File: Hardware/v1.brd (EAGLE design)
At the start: 77.5 x 32.6 mm, 64 parts, among them CN1 629105150521, CN2 TSW-120-08-L-S-RA, CN3 1734354-1, CN4 1-1734530-1, IC1 ADUM3160BRWZ, IC2 TUSB2046BIRHBT, IC3 IC_MAX3313, IC4 FT2232D, IC6 PCM2903C

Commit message: fixed some silkscreen issues
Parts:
- moved IC6 58.6 mm to (7.30, 24.9)
- moved R7 57.1 mm to (13.8, 28.1), turned to 0 degrees
- moved R6 41.8 mm to (13.8, 29.4), turned to 0 degrees
- moved C11 0.20 mm to (60.8, 24.9)
- moved C25 0.20 mm to (30.6, 27.4)
- moved C27 0.20 mm to (47.1, 30.9)
- moved C28 0.20 mm to (30.6, 24.9)
- moved R11 0.20 mm to (47.1, 23.9)
- moved C10 0.20 mm to (53.6, 29.7)
- moved C26 0.20 mm to (47.1, 26.7)
- moved C8 0.20 mm to (58.2, 24.1)
- moved C9 0.20 mm to (51.0, 29.7)
- moved IC2 0.20 mm to (52.4, 25.5)
- moved IC4 0.20 mm to (37.2, 26.5)
- moved R10 0.20 mm to (47.1, 22.5)
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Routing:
- net USB4_N: track 0.00 -> 43.5 mm, vias 0 -> 2
- net USB4_P: track 0.00 -> 43.0 mm, vias 0 -> 2
- net GND: track 22.9 -> 31.2 mm, vias 24 -> 32
- net DM4: track 0.00 -> 2.35 mm
- net DP4: track 0.00 -> 2.31 mm
- net ACC_COMMON: track 34.9 -> 34.1 mm

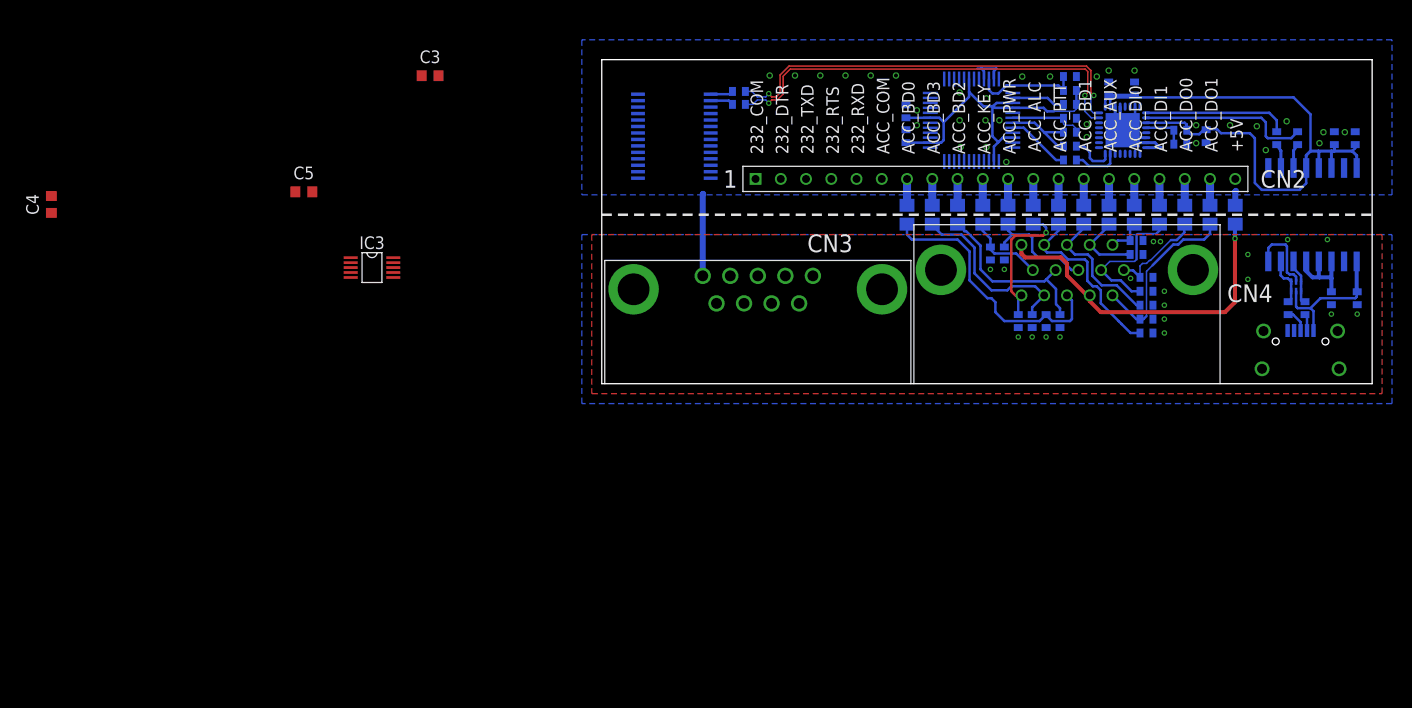
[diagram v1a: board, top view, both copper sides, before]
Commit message: added missing pullups to band lines
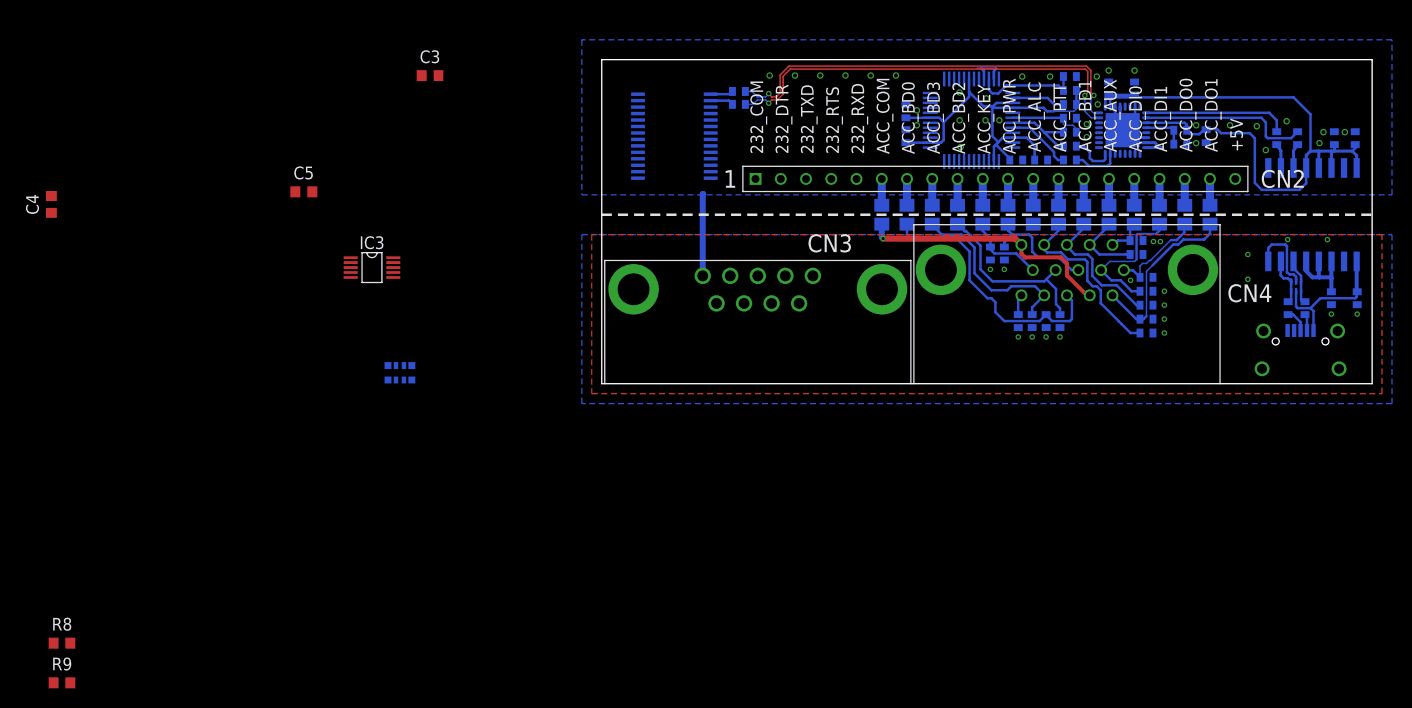
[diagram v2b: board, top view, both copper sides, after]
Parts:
- added C29: 100nF, rcl:C0402
- added C30: 1uF, rcl:C0402
- added R8: 69k8, rcl:R0603
- added R9: 100k, rcl:R0603
- added RN1: 2k2, m0wut:R_BOURNS_CAY16-J4
- C7: value 1uF -> 100nF
- moved L1 35.6 mm to (28.2, 17.0)
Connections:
- net +5V: now also C29.1, C30.1, R8.2, RN1.1, RN1.2, RN1.3, RN1.4
- net ACC_ALC: now also R9.2
- net ACC_BND0: now also RN1.3A
- net ACC_BND1: now also RN1.1A
- net ACC_BND2: now also RN1.2A
- net ACC_BND3: now also RN1.4A
- net ACC_COM: now also L1.1
- net GND: now also C29.2, C30.2, R9.1; no longer L1.1
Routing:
- net ALC_X: track 14.2 -> 2.07 mm, vias 1 -> 0
- net ACC_COMMON: track 34.1 -> 25.9 mm
- net +5V: track 38.4 -> 44.5 mm
- net ACC_COM: track 0.00 -> 2.65 mm
- net GND: track 31.2 -> 29.7 mm, vias 32 -> 31

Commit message: complete apart from sound card and PIC
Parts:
- added C31: 1uF, rcl:C0402
- added C32: 100nF, rcl:C0402
- C25: value 100nF -> 1uF
- C30: value 1uF -> 100nF
- R8, R9: device rcl:R0603 -> rcl:R0402
- moved R9 111.8 mm to (44.4, 22.5), flipped to the bottom
- moved R8 107.6 mm to (41.7, 22.5), flipped to the bottom
- moved RN1 53.0 mm to (27.5, 24.0), turned to 180 degrees
- moved C29 5.60 mm to (44.4, 28.1)
- moved C30 3.04 mm to (44.4, 23.9)
- moved R6 1.05 mm to (13.8, 30.4)
- moved R7 1.05 mm to (13.8, 29.1)
- moved IC6 1.00 mm to (7.30, 25.9)
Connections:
- net +5V: now also C31.1, C32.1
- net ACC_ALC: now also R8.1
- net ACC_BND0: now also RN1.1A; no longer RN1.3A
- net ACC_BND1: now also RN1.4A; no longer RN1.1A
- net ACC_BND2: now also RN1.3A; no longer RN1.2A
- net ACC_BND3: now also RN1.2A; no longer RN1.4A
- net GND: now also C31.2, C32.2
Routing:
- net ALC_X: track 2.07 -> 23.5 mm, vias 0 -> 1
- net ACC_BND1: track 2.65 -> 23.5 mm, vias 0 -> 1
- net +5V: track 44.5 -> 55.6 mm
- net ACC_BND2: track 2.65 -> 12.0 mm
- net ACC_BND3: track 2.65 -> 10.5 mm
- net ACC_BND0: track 2.65 -> 8.86 mm
- net ACC_ALC: track 2.65 -> 7.03 mm
- net DP2: track 8.02 -> 6.89 mm
- net USB4_P: track 43.0 -> 41.9 mm
- net USB4_N: track 43.5 -> 42.4 mm
- net N$37: track 5.37 -> 6.40 mm
- net DM2: track 6.68 -> 7.60 mm
- net GND: vias 31 -> 32
- added copper zone on layer 1, net GND

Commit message: destruction in the name of progress...
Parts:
- removed C3, C4, C5: 100nF, rcl:C0603
- removed IC6: PCM2903C, texas:SSOP28DB
- added C33, C34: 1nF, rcl:C0402
- added CAN1: SHIELDING_CAN, m0wut:CAN_LEADER_SMS462
- added D2: BZT52C3V0-7-F, adafruit:SOD-123
- added L2, L3, L4, L5, L6, L7: 100uH, m0wut:R0805
- added R12: 220, rcl:R0402
- CN1: value 629105150521 -> 54819-0519; device m0wut:USB_MICROB_WURTH -> m0wut:CONN_USB_MOLEX_MINI
- IC3: value IC_MAX3313 -> (none); device m0wut:IC_UMAX10 -> m0wut:SOT23-8L
- moved IC3 42.2 mm to (17.0, 24.9), flipped to the bottom, turned to 90 degrees
- moved R6 7.85 mm to (19.2, 36.1)
- moved R7 6.51 mm to (14.2, 35.6)
- moved C11 3.85 mm to (64.7, 24.9)
- moved C10 3.85 mm to (57.5, 29.7)
- moved C25 3.85 mm to (34.5, 27.4)
- moved C26 3.85 mm to (51.0, 26.7)
- moved C27 3.85 mm to (51.0, 30.9)
- moved C28 3.85 mm to (34.5, 24.9)
- moved C29 3.85 mm to (48.2, 28.1)
- moved C30 3.85 mm to (48.2, 23.9)
- moved C32 3.85 mm to (28.8, 24.0)
- moved C9 3.85 mm to (54.9, 29.7)
- moved IC2 3.85 mm to (56.2, 25.5)
- moved R10 3.85 mm to (51.0, 22.5)
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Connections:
- removed net 232_COM: CN2.P$1
- removed net AGNDC: IC6.11
- removed net AGNDP: IC6.18
- removed net AGNDX: IC6.22
- removed net DGND: IC6.26
- removed net DGNDU: IC6.4
- removed net N$8: C4.1, IC3.8
- removed net RS232(K2_TO_PIC): IC3.6
- removed net RS232(PIC_TO_K3): IC3.7
- removed net UART(K3_TO_PIC): IC3.5
- removed net UART(PIC_TO_K3): IC3.4
- removed net VBUS: IC6.3
- removed net VCCCI: IC6.10
- removed net VCCP2I: IC6.19
- removed net VCCXI: IC6.23
- removed net VCOM: IC6.14
- removed net VDDI: IC6.27
- new net 3V3_HUB: C10.1, C11.1, C9.1, IC2.25, IC2.26, IC2.3, L6.2, R5.1
- new net N$18: C33.1, CN3.2, L2.2
- new net N$188: IC3.1, L2.1
- new net N$189: D2.C, IC3.8, R12.1
- new net N$19: C6.1, C7.1, IC1.12, IC1.13, IC1.14, IC1.16, L5.1
- new net N$4: C34.1, CN3.3, L3.2
- new net USB_IN_GND: C1.2, C2.2, CN1.5, D1.2, IC1.2, IC1.8, L7.1
- net +3V3: now also L4.1, L5.2, L6.1; no longer C10.1, C11.1, C6.1, C7.1, C9.1, IC1.12, IC1.13, IC1.14, IC1.16, IC2.25, IC2.26, IC2.3, R5.1
- net +5V: now also IC3.7; no longer C5.1, IC3.1
- net AGND: now also C33.2, C34.2, CAN1.P$1, CAN1.P$10, CAN1.P$11, CAN1.P$12, CAN1.P$13, CAN1.P$14, CAN1.P$15, CAN1.P$16, CAN1.P$17, CAN1.P$18, CAN1.P$19, CAN1.P$2, CAN1.P$20, CAN1.P$21, CAN1.P$22, CAN1.P$23, CAN1.P$24, CAN1.P$25, CAN1.P$26, CAN1.P$27, CAN1.P$28, CAN1.P$29, CAN1.P$3, CAN1.P$30, CAN1.P$31, CAN1.P$32, CAN1.P$33, CAN1.P$34, CAN1.P$35, CAN1.P$36, CAN1.P$37, CAN1.P$38, CAN1.P$39, CAN1.P$4, CAN1.P$40, CAN1.P$41, CAN1.P$42, CAN1.P$43, CAN1.P$44, CAN1.P$45, CAN1.P$46, CAN1.P$47, CAN1.P$48, CAN1.P$49, CAN1.P$5, CAN1.P$50, CAN1.P$51, CAN1.P$52, CAN1.P$53, CAN1.P$54, CAN1.P$55, CAN1.P$56, CAN1.P$57, CAN1.P$58, CAN1.P$59, CAN1.P$6, CAN1.P$60, CAN1.P$61, CAN1.P$62, CAN1.P$63, CAN1.P$64, CAN1.P$65, CAN1.P$66, CAN1.P$67, CAN1.P$68, CAN1.P$7, CAN1.P$8, CAN1.P$9, CN1.TAB, CN1.TAB1, L7.2; no longer C1.2, C2.2, CN1.5, CN1.GND1, CN1.GND2, CN1.GND3, CN1.GND4, D1.2, IC1.2, IC1.8
- net DM4: no longer IC6.2
- net DP4: no longer IC6.1
- net GND: now also CN2.P$1, D2.A, IC3.2; no longer C4.2, C5.2, IC3.10
- net N$6: now also L3.1, R12.2; no longer C3.1, IC3.2
- net N$7: now also IC3.3, L4.2; no longer C3.2, IC3.9
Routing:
- net +3V3: track 68.1 -> 2.30 mm
- net USB4_N: track 42.4 -> 0.33 mm, vias 2 -> 0
- net USB4_P: track 41.9 -> 0.00 mm, vias 2 -> 0
- net 3V3_HUB: track 0.00 -> 18.2 mm
- net VCC: track 14.4 -> 2.27 mm
- net USB_IN_GND: track 0.00 -> 9.77 mm, vias 0 -> 11
- net N$188: track 0.00 -> 9.41 mm
- net AGND: track 7.80 -> 14.3 mm, vias 19 -> 8
- net N$6: track 0.00 -> 5.45 mm
- net N$4: track 0.00 -> 5.43 mm
- net N$18: track 0.00 -> 5.43 mm
- net N$189: track 0.00 -> 3.99 mm
- net DM0: track 17.2 -> 13.3 mm
- net DP0: track 14.6 -> 10.7 mm
- net ACC_BND1: track 23.5 -> 19.7 mm
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- added copper zone on layer 1, net USB_IN_GND
- added copper zone on layer 16, net USB_IN_GND
- removed copper zone on layer 1, net GND
- removed copper zone on layer 16, net GND
